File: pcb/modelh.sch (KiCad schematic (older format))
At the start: 42 parts, among them J1 USB_B, J2 Conn_01x16, J3 Conn_01x12, J4 Conn_01x04, J5 Conn_02x03_Odd_Even, J6 Conn_02x05_Odd_Even, SW1 SW_Push, U1 STM32F103C8Tx, U2 AMS1117-3.3, Y1 8MHz

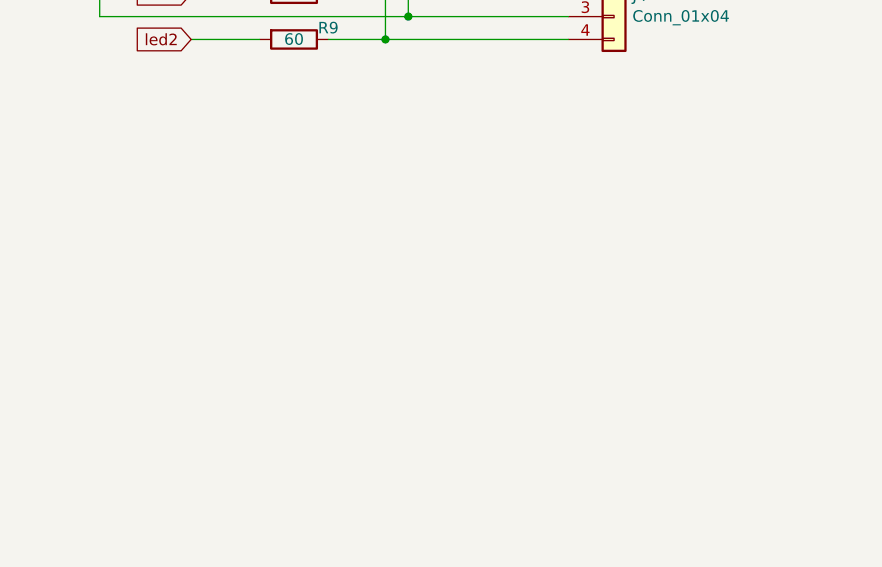
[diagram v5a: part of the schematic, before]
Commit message: Create testpoints for custom LEDs
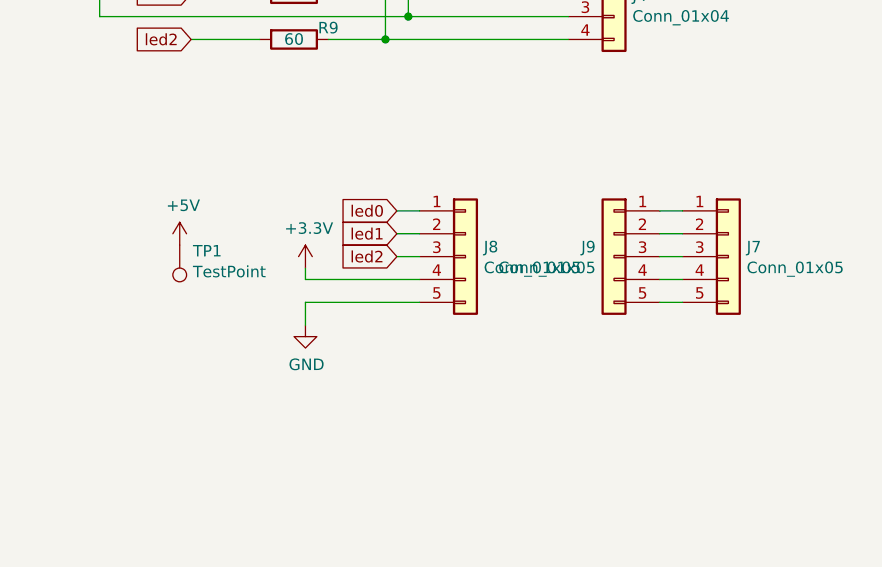
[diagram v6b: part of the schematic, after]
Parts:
- added J7, J8, J9: Conn_01x05, Connector_PinSocket_2.54mm:PinSocket_1x05_P2.54mm_Vertical, symbol Connector_Generic:Conn_01x05
- added TP1: TestPoint, TestPoint:TestPoint_THTPad_D1.5mm_Drill0.7mm, symbol Connector:TestPoint
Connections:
- net +3V3: now also J8.4 (Pin_4)
- net +5V: now also TP1.1
- net GND: now also J8.5 (Pin_5)
- net led0: now also J8.1 (Pin_1)
- net led1: now also J8.2 (Pin_2)
- net led2: now also J8.3 (Pin_3)
- new net: J7.1 (Pin_1), J9.1 (Pin_1)
- new net: J7.2 (Pin_2), J9.2 (Pin_2)
- new net: J7.3 (Pin_3), J9.3 (Pin_3)
- new net: J7.4 (Pin_4), J9.4 (Pin_4)
- new net: J7.5 (Pin_5), J9.5 (Pin_5)
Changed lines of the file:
@@
 Wire Wire Line
 	1450 5150 1250 5150
+Wire Wire Line
+	10600 5650 10500 5650
+Wire Wire Line
+	10600 5750 10500 5750
+Wire Wire Line
+	10500 5850 10600 5850
+Wire Wire Line
+	10600 5950 10500 5950
+Wire Wire Line
+	10600 6050 10500 6050
+$Comp
+L power:+3.3V #PWR0119
+U 1 1 5F15264C
+P 8950 5900
+F 0 "#PWR0119" H 8950 5750 50  0001 C CNN
+F 1 "+3.3V" H 8965 6073 50  0000 C CNN
+F 2 "" H 8950 5900 50  0001 C CNN
+F 3 "" H 8950 5900 50  0001 C CNN
+	1    8950 5900
+	1    0    0    -1
+$EndComp
+Text GLabel 9350 5650 0    50   Input ~ 0
+led0
+Text GLabel 9350 5750 0    50   Input ~ 0
+led1
+Text GLabel 9350 5850 0    50   Input ~ 0
+led2
+Wire Wire Line
+	8950 5950 8950 5900
+$Comp
+L power:GND #PWR0125
+U 1 1 5F1B8868
+P 8950 6150
+F 0 "#PWR0125" H 8950 5900 50  0001 C CNN
+F 1 "GND" H 8955 5977 50  0000 C CNN
+F 2 "" H 8950 6150 50  0001 C CNN
+F 3 "" H 8950 6150 50  0001 C CNN
+	1    8950 6150
+	1    0    0    -1
+$EndComp
+Wire Wire Line
+	8950 6050 8950 6150
+$Comp
+L Connector_Generic:Conn_01x05 J7
+U 1 1 5F225882
+P 10800 5850
+F 0 "J7" H 10880 5892 50  0000 L CNN
+F 1 "Conn_01x05" H 10880 5801 50  0000 L CNN
+F 2 "Connector_PinSocket_2.54mm:PinSocket_1x05_P2.54mm_Vertical" H 10800 5850 50  0001 C CNN
+F 3 "~" H 10800 5850 50  0001 C CNN
+	1    10800 5850
+	1    0    0    -1
+$EndComp
+$Comp
+L Connector:TestPoint TP1
+U 1 1 5F23CFEB
+P 8400 5800
+F 0 "TP1" H 8342 5826 50  0000 R CNN
+F 1 "TestPoint" H 8342 5917 50  0000 R CNN
+F 2 "TestPoint:TestPoint_THTPad_D1.5mm_Drill0.7mm" H 8600 5800 50  0001 C CNN
+F 3 "~" H 8600 5800 50  0001 C CNN
+	1    8400 5800
+	-1   0    0    1
+$EndComp
+$Comp
+L power:+5V #PWR0126
+U 1 1 5F25ACB8
+P 8400 5800
+F 0 "#PWR0126" H 8400 5650 50  0001 C CNN
+F 1 "+5V" H 8415 5973 50  0000 C CNN
+F 2 "" H 8400 5800 50  0001 C CNN
+F 3 "" H 8400 5800 50  0001 C CNN
+	1    8400 5800
+	1    0    0    -1
+$EndComp
+Wire Wire Line
+	9450 5650 9350 5650
+Wire Wire Line
+	9450 5750 9350 5750
+Wire Wire Line
+	9350 5850 9450 5850
+$Comp
+L Connector_Generic:Conn_01x05 J8
+U 1 1 5F2B29EC
+P 9650 5850
+F 0 "J8" H 9730 5892 50  0000 L CNN
+F 1 "Conn_01x05" H 9730 5801 50  0000 L CNN
+F 2 "Connector_PinSocket_2.54mm:PinSocket_1x05_P2.54mm_Vertical" H 9650 5850 50  0001 C CNN
+F 3 "~" H 9650 5850 50  0001 C CNN
+	1    9650 5850
+	1    0    0    -1
+$EndComp
+$Comp
+L Connector_Generic:Conn_01x05 J9
+U 1 1 5F2C10C8
+P 10300 5850
+F 0 "J9" H 10380 5892 50  0000 L CNN
+F 1 "Conn_01x05" H 10380 5801 50  0000 L CNN
+F 2 "Connector_PinSocket_2.54mm:PinSocket_1x05_P2.54mm_Vertical" H 10300 5850 50  0001 C CNN
+F 3 "~" H 10300 5850 50  0001 C CNN
+	1    10300 5850
+	-1   0    0    -1
+$EndComp
+Wire Wire Line
+	8950 5950 9450 5950
+Wire Wire Line
+	8950 6050 9450 6050
 $EndSCHEMATC

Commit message: WIP
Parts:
- R10, R5: value 1k -> 1.5k
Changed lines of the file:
@@
 P 2750 5150
 F 0 "R10" V 2543 5150 50  0000 C CNN
-F 1 "1k" V 2634 5150 50  0000 C CNN
+F 1 "1.5k" V 2634 5150 50  0000 C CNN
 F 2 "Resistor_SMD:R_0603_1608Metric" V 2680 5150 50  0001 C CNN
 F 3 "~" H 2750 5150 50  0001 C CNN
@@
 P 1700 5150
 F 0 "R5" V 1493 5150 50  0000 C CNN
-F 1 "1k" V 1584 5150 50  0000 C CNN
+F 1 "1.5k" V 1584 5150 50  0000 C CNN
 F 2 "Resistor_SMD:R_0603_1608Metric" V 1630 5150 50  0001 C CNN
 F 3 "~" H 1700 5150 50  0001 C CNN

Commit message: WIP
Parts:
- C1: value 100uF -> 10uF; LCSC (none) -> C19702
- C10, C11, C12, C13, C14: value 100 nF -> 100nF; LCSC (none) -> C1525
- C2, C4: LCSC (none) -> C1525
- C3: value 330uF -> 10uF; LCSC (none) -> C19702
- C9: footprint Capacitor_SMD:C_0603_1608Metric -> Capacitor_SMD:C_0402_1005Metric; LCSC (none) -> C1525
- LED2: value amber -> green
- R10, R11, R5: LCSC (none) -> C22843
- R12, R13, R14, R15, R16: LCSC (none) -> C17477
- R17, R18: LCSC (none) -> C25803
- R6: LCSC C21190 -> C22935
- R7, R8, R9: LCSC C22787 -> C17408
- U1: LCSC (none) -> C8734
- U2: LCSC (none) -> C6186
- Y1: LCSC (none) -> C115962
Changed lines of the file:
@@
 F 2 "Resistor_SMD:R_0805_2012Metric" V 8830 4600 50  0001 C CNN
 F 3 "~" H 8900 4600 50  0001 C CNN
-F 4 "C22787" H 8900 4600 50  0001 C CNN "LCSC"
+F 4 "C17408" H 8900 4600 50  0001 C CNN "LCSC"
 	1    8900 4600
 	0    1    1    0
@@
 F 2 "Resistor_SMD:R_0805_2012Metric" V 8830 4700 50  0001 C CNN
 F 3 "~" H 8900 4700 50  0001 C CNN
-F 4 "C22787" H 8900 4700 50  0001 C CNN "LCSC"
+F 4 "C17408" H 8900 4700 50  0001 C CNN "LCSC"
 	1    8900 4700
 	0    1    1    0
@@
 F 2 "Resistor_SMD:R_0805_2012Metric" V 8830 4900 50  0001 C CNN
 F 3 "~" H 8900 4900 50  0001 C CNN
-F 4 "C22787" H 8900 4900 50  0001 C CNN "LCSC"
+F 4 "C17408" H 8900 4900 50  0001 C CNN "LCSC"
 	1    8900 4900
 	0    1    1    0
@@
 F 2 "Package_QFP:LQFP-48_7x7mm_P0.5mm" H 5200 2300 50  0001 R CNN
 F 3 "http://www.st.com/st-web-ui/static/active/en/resource/technical/document/datasheet/CD00161566.pdf" H 5800 3700 50  0001 C CNN
+F 4 "C8734" H 5800 3700 50  0001 C CNN "LCSC"
 	1    5800 3700
 	1    0    0    -1
@@
 F 2 "Crystal:Crystal_SMD_5032-2Pin_5.0x3.2mm" H 5650 6600 50  0001 C CNN
 F 3 "~" H 5650 6600 50  0001 C CNN
+F 4 "C115962" H 5650 6600 50  0001 C CNN "LCSC"
 	1    5650 6600
 	0    1    1    0
@@
 F 2 "Resistor_SMD:R_0603_1608Metric" V 6030 6600 50  0001 C CNN
 F 3 "~" H 6100 6600 50  0001 C CNN
-F 4 "C21190" H 6100 6600 50  0001 C CNN "LCSC"
+F 4 "C22935" H 6100 6600 50  0001 C CNN "LCSC"
 	1    6100 6600
 	1    0    0    -1
@@
 P 1450 7000
 F 0 "LED2" V 1489 6883 50  0000 R CNN
-F 1 "amber" V 1398 6883 50  0000 R CNN
+F 1 "green" V 1398 6883 50  0000 R CNN
 F 2 "LED_SMD:LED_0805_2012Metric" H 1450 7000 50  0001 C CNN
 F 3 "~" H 1450 7000 50  0001 C CNN
@@
 F 2 "Package_TO_SOT_SMD:SOT-223-3_TabPin2" H 2350 3700 50  0001 C CNN
 F 3 "http://www.advanced-monolithic.com/pdf/ds1117.pdf" H 2450 3250 50  0001 C CNN
+F 4 "C6186" H 2350 3500 50  0001 C CNN "LCSC"
 	1    2350 3500
 	1    0    0    -1
@@
 F 2 "Capacitor_SMD:C_0402_1005Metric" H 1788 3500 50  0001 C CNN
 F 3 "~" H 1750 3650 50  0001 C CNN
+F 4 "C1525" H 1750 3650 50  0001 C CNN "LCSC"
 	1    1750 3650
 	1    0    0    -1
@@
 P 1300 3650
 F 0 "C1" H 1415 3696 50  0000 L CNN
-F 1 "100uF" H 1415 3605 50  0000 L CNN
+F 1 "10uF" H 1415 3605 50  0000 L CNN
 F 2 "Capacitor_SMD:C_0603_1608Metric" H 1338 3500 50  0001 C CNN
 F 3 "~" H 1300 3650 50  0001 C CNN
+F 4 "C19702" H 1300 3650 50  0001 C CNN "LCSC"
 	1    1300 3650
 	1    0    0    -1
@@
 F 2 "Capacitor_SMD:C_0402_1005Metric" H 3338 3500 50  0001 C CNN
 F 3 "~" H 3300 3650 50  0001 C CNN
+F 4 "C1525" H 3300 3650 50  0001 C CNN "LCSC"
 	1    3300 3650
 	1    0    0    -1
@@
 P 2850 3650
 F 0 "C3" H 2965 3696 50  0000 L CNN
-F 1 "330uF" H 2965 3605 50  0000 L CNN
+F 1 "10uF" H 2965 3605 50  0000 L CNN
 F 2 "Capacitor_SMD:C_0603_1608Metric" H 2888 3500 50  0001 C CNN
 F 3 "~" H 2850 3650 50  0001 C CNN
+F 4 "C19702" H 2850 3650 50  0001 C CNN "LCSC"
 	1    2850 3650
 	1    0    0    -1
@@
 F 0 "C9" H 3965 6996 50  0000 L CNN
 F 1 "100nF" H 3965 6905 50  0000 L CNN
-F 2 "Capacitor_SMD:C_0603_1608Metric" H 3888 6800 50  0001 C CNN
+F 2 "Capacitor_SMD:C_0402_1005Metric" H 3888 6800 50  0001 C CNN
 F 3 "~" H 3850 6950 50  0001 C CNN
+F 4 "C1525" H 3850 6950 50  0001 C CNN "LCSC"
 	1    3850 6950
 	1    0    0    -1
@@
 F 2 "Resistor_SMD:R_0603_1608Metric" V 2680 5150 50  0001 C CNN
 F 3 "~" H 2750 5150 50  0001 C CNN
+F 4 "C22843" H 2750 5150 50  0001 C CNN "LCSC"
 	1    2750 5150
 	0    1    1    0
@@
 F 2 "Resistor_SMD:R_0603_1608Metric" V 1630 5150 50  0001 C CNN
 F 3 "~" H 1700 5150 50  0001 C CNN
+F 4 "C22843" H 1700 5150 50  0001 C CNN "LCSC"
 	1    1700 5150
 	0    1    1    0
@@
 P 3800 1300
 F 0 "C10" H 3915 1346 50  0000 L CNN
-F 1 "100 nF" H 3915 1255 50  0000 L CNN
+F 1 "100nF" H 3915 1255 50  0000 L CNN
 F 2 "Capacitor_SMD:C_0402_1005Metric" H 3838 1150 50  0001 C CNN
 F 3 "~" H 3800 1300 50  0001 C CNN
+F 4 "C1525" H 3800 1300 50  0001 C CNN "LCSC"
 	1    3800 1300
 	1    0    0    -1
@@
 P 4300 1300
 F 0 "C11" H 4415 1346 50  0000 L CNN
-F 1 "100 nF" H 4415 1255 50  0000 L CNN
+F 1 "100nF" H 4415 1255 50  0000 L CNN
 F 2 "Capacitor_SMD:C_0402_1005Metric" H 4338 1150 50  0001 C CNN
 F 3 "~" H 4300 1300 50  0001 C CNN
+F 4 "C1525" H 4300 1300 50  0001 C CNN "LCSC"
 	1    4300 1300
 	1    0    0    -1
@@
 P 4800 1300
 F 0 "C12" H 4915 1346 50  0000 L CNN
-F 1 "100 nF" H 4915 1255 50  0000 L CNN
+F 1 "100nF" H 4915 1255 50  0000 L CNN
 F 2 "Capacitor_SMD:C_0402_1005Metric" H 4838 1150 50  0001 C CNN
 F 3 "~" H 4800 1300 50  0001 C CNN
+F 4 "C1525" H 4800 1300 50  0001 C CNN "LCSC"
 	1    4800 1300
 	1    0    0    -1
@@
 P 5300 1300
 F 0 "C13" H 5415 1346 50  0000 L CNN
-F 1 "100 nF" H 5415 1255 50  0000 L CNN
+F 1 "100nF" H 5415 1255 50  0000 L CNN
 F 2 "Capacitor_SMD:C_0402_1005Metric" H 5338 1150 50  0001 C CNN
 F 3 "~" H 5300 1300 50  0001 C CNN
+F 4 "C1525" H 5300 1300 50  0001 C CNN "LCSC"
 	1    5300 1300
 	1    0    0    -1
@@
 P 5800 1300
 F 0 "C14" H 5915 1346 50  0000 L CNN
-F 1 "100 nF" H 5915 1255 50  0000 L CNN
+F 1 "100nF" H 5915 1255 50  0000 L CNN
 F 2 "Capacitor_SMD:C_0402_1005Metric" H 5838 1150 50  0001 C CNN
 F 3 "~" H 5800 1300 50  0001 C CNN
+F 4 "C1525" H 5800 1300 50  0001 C CNN "LCSC"
 	1    5800 1300
 	1    0    0    -1
@@
 F 2 "Resistor_SMD:R_0603_1608Metric" V 2330 1100 50  0001 C CNN
 F 3 "~" H 2400 1100 50  0001 C CNN
+F 4 "C22843" H 2400 1100 50  0001 C CNN "LCSC"
 	1    2400 1100
 	-1   0    0    1
@@
 F 2 "Resistor_SMD:R_0805_2012Metric_Pad1.15x1.40mm_HandSolder" H 9800 4000 50  0001 C CNN
 F 3 "~" H 9800 4000 50  0001 C CNN
+F 4 "C17477" H 9800 4000 50  0001 C CNN "LCSC"
 	1    9800 4000
 	0    1    1    0
@@
 F 2 "Resistor_SMD:R_0805_2012Metric_Pad1.15x1.40mm_HandSolder" H 9800 4100 50  0001 C CNN
 F 3 "~" H 9800 4100 50  0001 C CNN
+F 4 "C17477" H 9800 4100 50  0001 C CNN "LCSC"
 	1    9800 4100
 	0    1    1    0
@@
 F 2 "Resistor_SMD:R_0805_2012Metric_Pad1.15x1.40mm_HandSolder" H 9800 4200 50  0001 C CNN
 F 3 "~" H 9800 4200 50  0001 C CNN
+F 4 "C17477" H 9800 4200 50  0001 C CNN "LCSC"
 	1    9800 4200
 	0    1    1    0
@@
 F 2 "Resistor_SMD:R_0805_2012Metric_Pad1.15x1.40mm_HandSolder" H 9800 4300 50  0001 C CNN
 F 3 "~" H 9800 4300 50  0001 C CNN
+F 4 "C17477" H 9800 4300 50  0001 C CNN "LCSC"
 	1    9800 4300
 	0    1    1    0
@@
 F 2 "Resistor_SMD:R_0805_2012Metric_Pad1.15x1.40mm_HandSolder" V 1880 1100 50  0001 C CNN
 F 3 "~" H 1950 1100 50  0001 C CNN
+F 4 "C17477" H 1950 1100 50  0001 C CNN "LCSC"
 	1    1950 1100
 	0    1    1    0
@@
 F 2 "Resistor_SMD:R_0603_1608Metric" V 2680 5450 50  0001 C CNN
 F 3 "~" H 2750 5450 50  0001 C CNN
+F 4 "C25803" H 2750 5450 50  0001 C CNN "LCSC"
 	1    2750 5450
 	0    1    1    0
@@
 F 2 "Resistor_SMD:R_0603_1608Metric" V 1630 5450 50  0001 C CNN
 F 3 "~" H 1700 5450 50  0001 C CNN
+F 4 "C25803" H 1700 5450 50  0001 C CNN "LCSC"
 	1    1700 5450
 	0    -1   1    0
